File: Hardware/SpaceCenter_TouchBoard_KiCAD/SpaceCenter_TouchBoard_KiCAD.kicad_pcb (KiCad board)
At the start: 2 copper layers, 19.1 x 19.1 mm, 6 parts, among them J1 Conn_01x05_Male, J2 TOUCH_SENSOR

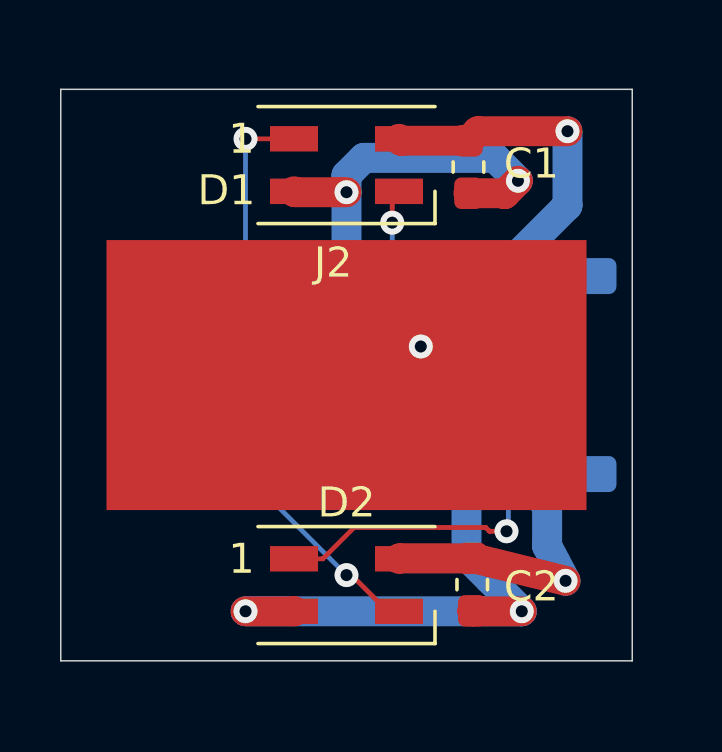
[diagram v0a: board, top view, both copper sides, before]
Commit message: Updated Touch Board with new connector
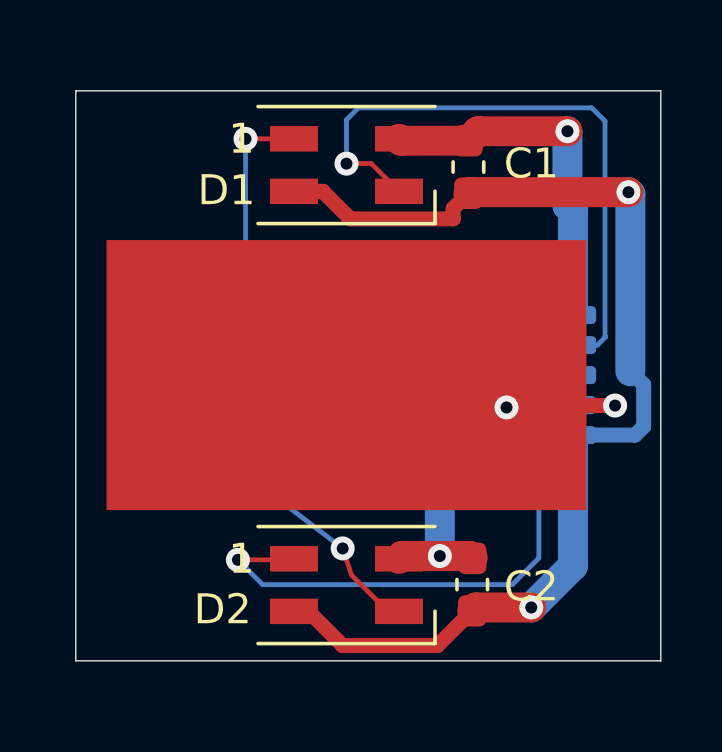
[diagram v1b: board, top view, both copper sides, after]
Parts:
- J1: footprint Connector_JST:JST_SH_SM05B-SRSS-TB_1x05-1MP_P1.00mm_Horizontal -> Connector_JST:JST_SH_BM05B-SRSS-TB_1x05-1MP_P1.00mm_Vertical
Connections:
- J1 pad 2: CAP_TOUCH -> DATA_IN
- J1 pad 4: DATA_IN -> CAP_TOUCH
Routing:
- net DATA_IN: track 9.29 -> 21.3 mm
- net DATA_OUT: track 13.8 -> 20.0 mm
- net +5V: track 29.9 -> 25.6 mm
- net GND: track 40.7 -> 37.8 mm, vias 4 -> 2
- net CAP_TOUCH: track 2.25 -> 5.06 mm, vias 1 -> 2
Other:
- board size 19.1 x 19.1 mm -> 19.5 x 19 mm
- board text added: "Touch Board 1.0 AC"

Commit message: TouchBoard updated and ordered
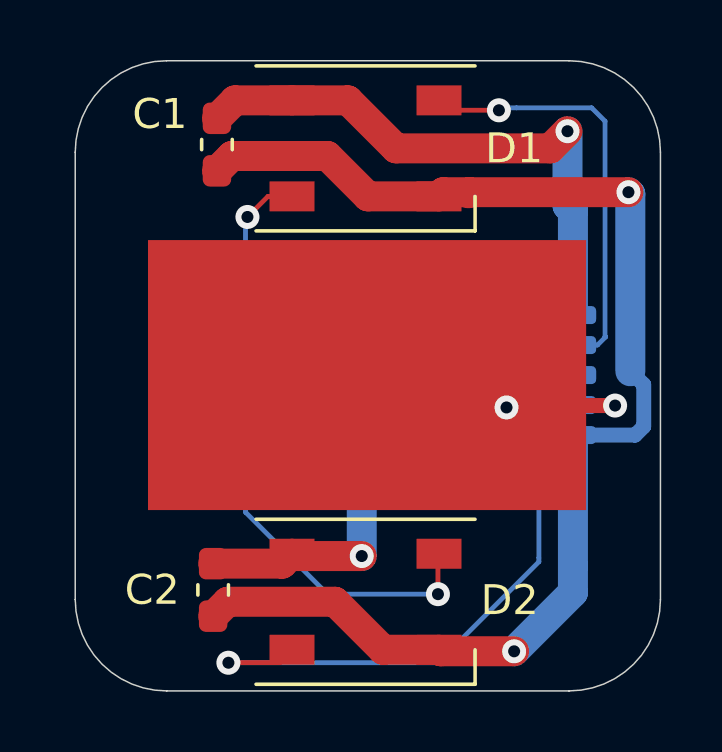
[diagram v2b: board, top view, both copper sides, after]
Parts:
- D1, D2: value SK6812MINI -> SK6812; footprint LED_SMD:LED_SK6812MINI_PLCC4_3.5x3.5mm_P1.75mm -> LED_SMD:LED_SK6812_PLCC4_5.0x5.0mm_P3.2mm
- moved C2 8.64 mm to (132.1, 103.7)
- moved C1 8.42 mm to (132.2, 88.9)
- moved D1 0.84 mm to (137.2, 89.0)
- moved D2 0.84 mm to (137.2, 104.1)
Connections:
- D1 pad 1: Net-(D1-Pad1) -> GND
- D1 pad 2: GND -> DATA_IN
- D1 pad 3: DATA_IN -> +5V
- D1 pad 4: +5V -> Net-(D1-Pad4)
- D2 pad 1: DATA_OUT -> GND
- D2 pad 2: GND -> Net-(D1-Pad4)
- D2 pad 3: Net-(D1-Pad1) -> +5V
- D2 pad 4: +5V -> DATA_OUT
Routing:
- net Net-(D1-Pad4): track 0.00 -> 20.5 mm, vias 0 -> 2
- net Net-(D1-Pad1): track 19.9 -> 0.00 mm, vias 2 -> 0
- net +5V: track 25.6 -> 36.3 mm
- net DATA_IN: track 21.3 -> 14.3 mm
- net GND: track 37.8 -> 44.0 mm
- net DATA_OUT: track 20.0 -> 21.5 mm
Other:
- board size 19.5 x 19 mm -> 19.5 x 21 mm
- board text added: "Touch Board 1.1 AC"
- board text removed: "Touch Board 1.0 AC"
